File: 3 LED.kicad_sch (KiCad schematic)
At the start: 14 parts, among them J1 Conn_01x04_Socket, Q1 NPN, Q2 NPN, Q3 NPN, U1 74HC238

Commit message: On Production
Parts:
- removed U2, U3: ~, Library_Custom:LEGO HOLE 4.5-6.5, symbol Library_Custom:M3_Hole
- C1: footprint (none) -> Capacitor_SMD:C_0805_2012Metric
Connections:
- net at D2.2 (A): now also R2.2; no longer R3.2
- net at D3.2 (A): now also R3.2; no longer R2.2
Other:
- moved on the sheet: D2, D3
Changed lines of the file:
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@@
     (stroke (width 0) (type default))
   )
-  (wire (pts (xy 190.5 111.76) (xy 199.39 111.76))
+  (wire (pts (xy 191.77 111.76) (xy 199.39 111.76))
     (stroke (width 0) (type default))
   )
@@
     (stroke (width 0) (type default))
   )
+  (wire (pts (xy 191.77 123.19) (xy 199.39 123.19))
+    (stroke (width 0) (type default))
+  )
   (wire (pts (xy 109.22 81.28) (xy 118.11 81.28))
     (stroke (width 0) (type default))
@@
     (stroke (width 0) (type default))
   )
-  (wire (pts (xy 179.07 123.19) (xy 182.88 123.19))
-    (stroke (width 0) (type default))
-  )
   (wire (pts (xy 199.39 101.6) (xy 199.39 111.76))
     (stroke (width 0) (type default))
@@
     (stroke (width 0) (type default))
   )
+  (wire (pts (xy 179.07 123.19) (xy 184.15 123.19))
+    (stroke (width 0) (type default))
+  )
   (wire (pts (xy 99.06 97.79) (xy 99.06 100.33))
     (stroke (width 0) (type default))
@@
     (stroke (width 0) (type default))
   )
-  (wire (pts (xy 199.39 123.19) (xy 190.5 123.19))
-    (stroke (width 0) (type default))
-  )
   (wire (pts (xy 90.17 130.81) (xy 101.6 130.81))
     (stroke (width 0) (type default))
@@
     (stroke (width 0) (type default))
   )
-  (wire (pts (xy 179.07 111.76) (xy 182.88 111.76))
+  (wire (pts (xy 179.07 111.76) (xy 184.15 111.76))
     (stroke (width 0) (type default))
   )
@@
       (effects (font (size 1.27 1.27)) (justify left))
     )
-    (property "Footprint" "" (at 91.1352 138.43 0)
+    (property "Footprint" "Capacitor_SMD:C_0805_2012Metric" (at 91.1352 138.43 0)
       (effects (font (size 1.27 1.27)) hide)
     )
@@
     )
   )
-  (symbol (lib_id "Device:LED") (at 186.69 123.19 180) (unit 1)
-    (in_bom yes) (on_board yes) (dnp no) (fields_autoplaced)
-    (property "Reference" "D2" (at 188.2775 129.54 0)
-      (effects (font (size 1.27 1.27)))
-    )
-    (property "Value" "LED" (at 188.2775 127 0)
-      (effects (font (size 1.27 1.27)))
-    )
-    (property "Footprint" "LED_THT:LED_D10.0mm" (at 186.69 123.19 0)
-      (effects (font (size 1.27 1.27)) hide)
-    )
-    (property "Datasheet" "~" (at 186.69 123.19 0)
+  (symbol (lib_id "Device:LED") (at 187.96 111.76 180) (unit 1)
+    (in_bom yes) (on_board yes) (dnp no) (fields_autoplaced)
+    (property "Reference" "D2" (at 189.5475 118.11 0)
+      (effects (font (size 1.27 1.27)))
+    )
+    (property "Value" "LED" (at 189.5475 115.57 0)
+      (effects (font (size 1.27 1.27)))
+    )
+    (property "Footprint" "LED_THT:LED_D10.0mm" (at 187.96 111.76 0)
+      (effects (font (size 1.27 1.27)) hide)
+    )
+    (property "Datasheet" "~" (at 187.96 111.76 0)
       (effects (font (size 1.27 1.27)) hide)
     )
@@
     )
   )
-  (symbol (lib_id "Library_Custom:M3_Hole") (at 83.82 156.21 0) (unit 1)
-    (in_bom yes) (on_board yes) (dnp no) (fields_autoplaced)
-    (property "Reference" "U2" (at 88.9 158.6258 0)
-      (effects (font (size 1.27 1.27)) (justify left))
-    )
-    (property "Value" "~" (at 83.82 156.21 0)
-      (effects (font (size 1.27 1.27)))
-    )
-    (property "Footprint" "Library_Custom:LEGO HOLE 4.5-6.5" (at 83.82 156.21 0)
-      (effects (font (size 1.27 1.27)) hide)
-    )
-    (property "Datasheet" "" (at 83.82 156.21 0)
-      (effects (font (size 1.27 1.27)) hide)
-    )
-    (instances
-      (project "3 LED"
-        (path "/03a97cb7-bbff-478c-a2ff-11a3010c6cde"
-          (reference "U2") (unit 1)
-        )
-      )
-    )
-  )
   (symbol (lib_id "Device:LED") (at 186.69 101.6 180) (unit 1)
     (in_bom yes) (on_board yes) (dnp no) (fields_autoplaced)
@@
     )
   )
-  (symbol (lib_id "Device:LED") (at 186.69 111.76 180) (unit 1)
-    (in_bom yes) (on_board yes) (dnp no) (fields_autoplaced)
-    (property "Reference" "D3" (at 188.2775 118.11 0)
-      (effects (font (size 1.27 1.27)))
-    )
-    (property "Value" "LED" (at 188.2775 115.57 0)
-      (effects (font (size 1.27 1.27)))
-    )
-    (property "Footprint" "LED_THT:LED_D10.0mm" (at 186.69 111.76 0)
-      (effects (font (size 1.27 1.27)) hide)
-    )
-    (property "Datasheet" "~" (at 186.69 111.76 0)
+  (symbol (lib_id "Device:LED") (at 187.96 123.19 180) (unit 1)
+    (in_bom yes) (on_board yes) (dnp no) (fields_autoplaced)
+    (property "Reference" "D3" (at 189.5475 129.54 0)
+      (effects (font (size 1.27 1.27)))
+    )
+    (property "Value" "LED" (at 189.5475 127 0)
+      (effects (font (size 1.27 1.27)))
+    )
+    (property "Footprint" "LED_THT:LED_D10.0mm" (at 187.96 123.19 0)
+      (effects (font (size 1.27 1.27)) hide)
+    )
+    (property "Datasheet" "~" (at 187.96 123.19 0)
       (effects (font (size 1.27 1.27)) hide)
     )
@@
         )
       )
-    )
-  )
-  (symbol (lib_id "Library_Custom:M3_Hole") (at 100.33 156.21 0) (unit 1)
-    (in_bom yes) (on_board yes) (dnp no) (fields_autoplaced)
-    (property "Reference" "U3" (at 105.41 158.6258 0)
-      (effects (font (size 1.27 1.27)) (justify left))
-    )
-    (property "Value" "~" (at 100.33 156.21 0)
-      (effects (font (size 1.27 1.27)))
-    )
-    (property "Footprint" "Library_Custom:LEGO HOLE 4.5-6.5" (at 100.33 156.21 0)
-      (effects (font (size 1.27 1.27)) hide)
-    )
-    (property "Datasheet" "" (at 100.33 156.21 0)
-      (effects (font (size 1.27 1.27)) hide)
-    )
-    (instances
-      (project "3 LED"
-        (path "/03a97cb7-bbff-478c-a2ff-11a3010c6cde"
-          (reference "U3") (unit 1)
-        )
-      )

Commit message: Production Version
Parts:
- added JP1, JP2, JP3: Jumper_2_Open, SofleRGB:Jumper, symbol Jumper:Jumper_2_Open
- added R4, R5, R6, R7, R8, R9: R, Resistor_SMD:R_0603_1608Metric, symbol Device:R
- U1: value 74HC238 -> 74HC238D
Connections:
- net +5V: now also D1.2 (A), D2.2 (A), D3.2 (A), J1.2 (Pin_2); no longer J1.3 (Pin_3), Q1.1 (C), Q2.1 (C), Q3.1 (C)
- net GND: now also J1.1 (Pin_1), Q1.3 (E), Q2.3 (E), Q3.3 (E), R7.2, R8.2, R9.2; no longer D1.1 (K), D2.1 (K), D3.1 (K), J1.4 (Pin_4)
- net L1: now also JP1.2 (B), R4.1; no longer Q1.2 (B)
- net L2: now also JP2.2 (B), R5.1; no longer Q2.2 (B)
- net L3: now also JP3.1 (A), R6.1; no longer Q3.2 (B)
- net S0: now also J1.4 (Pin_4); no longer J1.2 (Pin_2)
- net S1: now also J1.3 (Pin_3); no longer J1.1 (Pin_1)
- net at R2.1: now also D2.1 (K); no longer Q2.3 (E)
- net at R2.2: now also Q2.1 (C), JP2.1 (A); no longer D2.2 (A)
- net at R1.1: now also D1.1 (K); no longer Q1.3 (E)
- net at R3.1: now also D3.1 (K); no longer Q3.3 (E)
- net at R3.2: now also Q3.1 (C), JP3.2 (B); no longer D3.2 (A)
- net at R1.2: now also Q1.1 (C), JP1.1 (A); no longer D1.2 (A)
- new net: Q2.2 (B), R5.2, R8.1
- new net: Q1.2 (B), R4.2, R7.1
- new net: Q3.2 (B), R6.2, R9.1
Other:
- moved on the sheet: D1, D2, D3, J1, Q1, Q2, Q3, R1, R2, R3

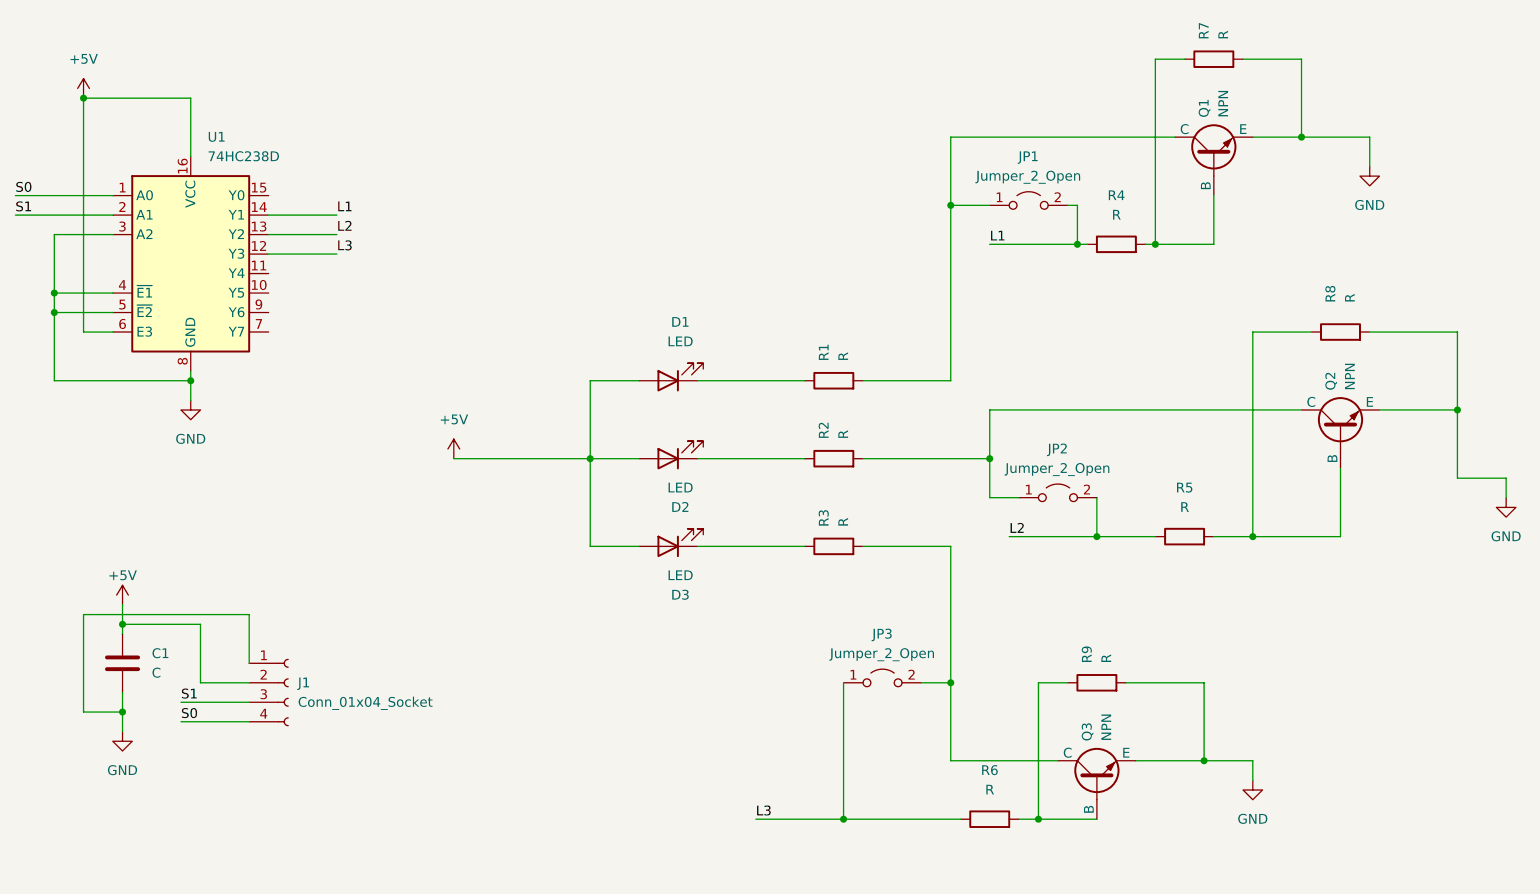
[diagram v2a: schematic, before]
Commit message: update: 74HC138D
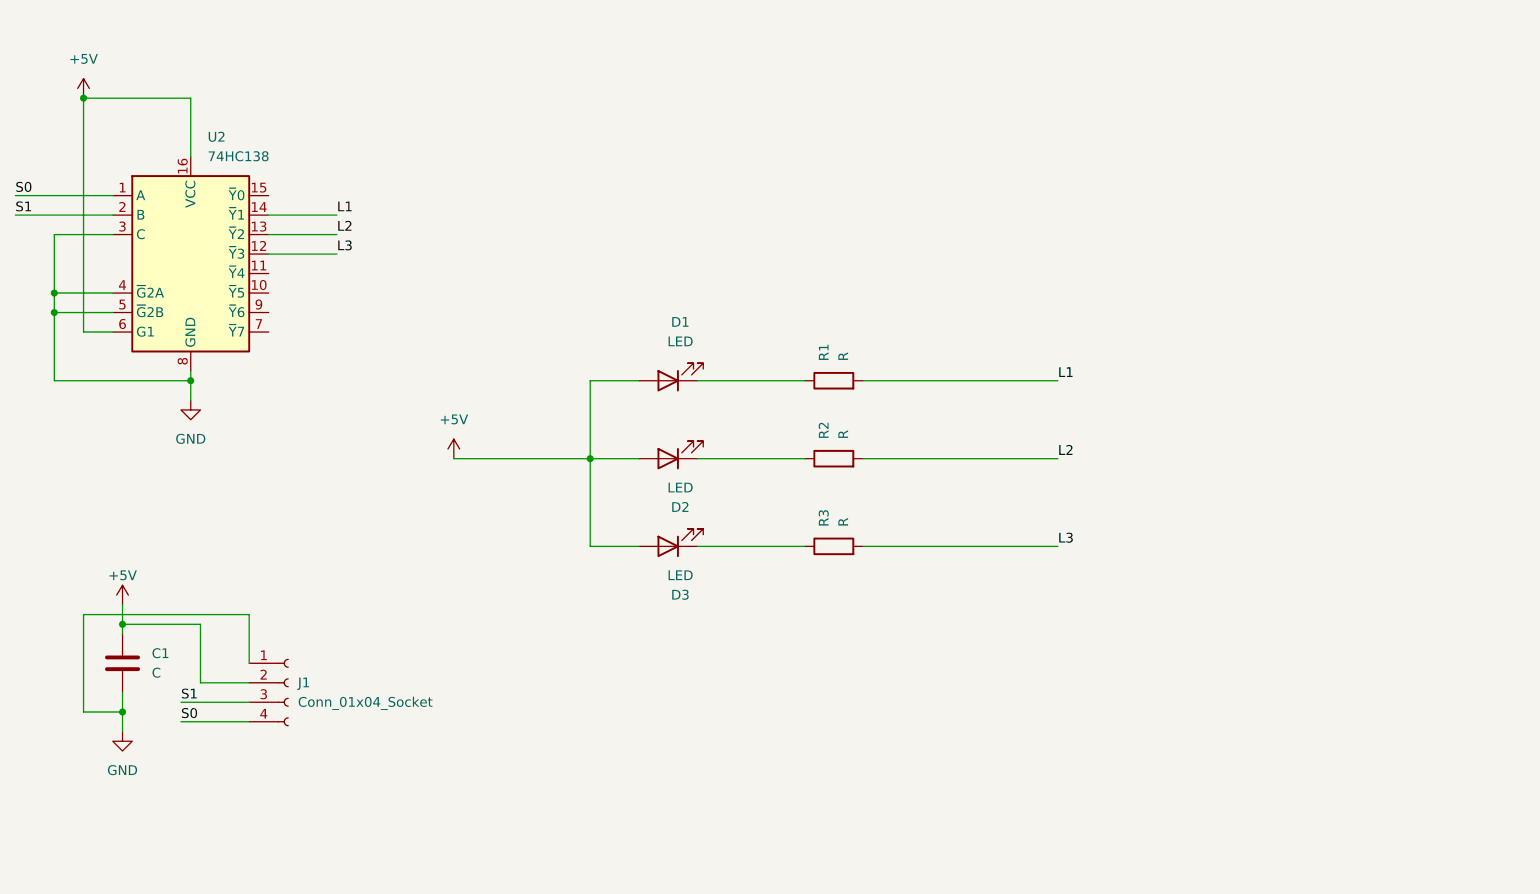
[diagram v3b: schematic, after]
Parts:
- removed JP1, JP2, JP3: Jumper_2_Open, SofleRGB:Jumper, symbol Jumper:Jumper_2_Open
- removed Q1, Q2, Q3: NPN, Package_TO_SOT_SMD:SOT-23-3, symbol Simulation_SPICE:NPN
- removed R4, R5, R6, R7, R8, R9: R, Resistor_SMD:R_0603_1608Metric, symbol Device:R
- removed U1: 74HC238D, Package_SO:SOP-16_3.9x9.9mm_P1.27mm, symbol 74xx:74HC238
- added U2: 74HC138, Package_SO:SOP-16_3.9x9.9mm_P1.27mm, symbol 74xx:74HC138
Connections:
- net +5V: now also U2.16 (VCC), U2.6 (G1)
- net GND: now also U2.3 (C), U2.4 (~{G}2A), U2.5 (~{G}2B), U2.8 (GND)
- net L1: now also R1.2, U2.14 (~{Y}1)
- net L2: now also R2.2, U2.13 (~{Y}2)
- net L3: now also R3.2, U2.12 (~{Y}3)
- net S0: now also U2.1 (A)
- net S1: now also U2.2 (B)

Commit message: update label
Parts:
- C1: value C -> 100nf
- R1, R2: value R -> 100
- R3: value R -> 160
- U2: value 74HC138 -> 74HC138D
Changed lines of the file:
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@@
       (effects (font (size 1.27 1.27)) (justify left))
     )
-    (property "Value" "C" (at 93.98 135.89 0)
+    (property "Value" "100nf" (at 93.98 135.89 0)
       (effects (font (size 1.27 1.27)) (justify left))
     )
@@
       (effects (font (size 1.27 1.27)) (justify left))
     )
-    (property "Value" "74HC138" (at 101.2541 68.58 0)
+    (property "Value" "74HC138D" (at 101.2541 68.58 0)
       (effects (font (size 1.27 1.27)) (justify left))
     )
@@
   (symbol (lib_id "Device:R") (at 182.88 119.38 90) (unit 1)
     (in_bom yes) (on_board yes) (dnp no) (fields_autoplaced)
-    (property "Reference" "R3" (at 181.61 116.84 0)
-      (effects (font (size 1.27 1.27)) (justify left))
-    )
-    (property "Value" "R" (at 184.15 116.84 0)
-      (effects (font (size 1.27 1.27)) (justify left))
+    (property "Reference" "R3" (at 182.88 113.03 90)
+      (effects (font (size 1.27 1.27)))
+    )
+    (property "Value" "160" (at 182.88 115.57 90)
+      (effects (font (size 1.27 1.27)))
     )
     (property "Footprint" "Resistor_SMD:R_0603_1608Metric" (at 182.88 121.158 90)
@@
   (symbol (lib_id "Device:R") (at 182.88 107.95 90) (unit 1)
     (in_bom yes) (on_board yes) (dnp no) (fields_autoplaced)
-    (property "Reference" "R2" (at 181.61 105.41 0)
-      (effects (font (size 1.27 1.27)) (justify left))
-    )
-    (property "Value" "R" (at 184.15 105.41 0)
-      (effects (font (size 1.27 1.27)) (justify left))
+    (property "Reference" "R2" (at 182.88 101.6 90)
+      (effects (font (size 1.27 1.27)))
+    )
+    (property "Value" "100" (at 182.88 104.14 90)
+      (effects (font (size 1.27 1.27)))
     )
     (property "Footprint" "Resistor_SMD:R_0603_1608Metric" (at 182.88 109.728 90)
@@
   (symbol (lib_id "Device:R") (at 182.88 97.79 90) (unit 1)
     (in_bom yes) (on_board yes) (dnp no) (fields_autoplaced)
-    (property "Reference" "R1" (at 181.61 95.25 0)
-      (effects (font (size 1.27 1.27)) (justify left))
-    )
-    (property "Value" "R" (at 184.15 95.25 0)
-      (effects (font (size 1.27 1.27)) (justify left))
+    (property "Reference" "R1" (at 182.88 91.44 90)
+      (effects (font (size 1.27 1.27)))
+    )
+    (property "Value" "100" (at 182.88 93.98 90)
+      (effects (font (size 1.27 1.27)))
     )
     (property "Footprint" "Resistor_SMD:R_0603_1608Metric" (at 182.88 99.568 90)
